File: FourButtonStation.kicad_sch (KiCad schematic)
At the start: 63 parts, among them J1 AC IN, J10 AC IN, J2 External 3V, J3 UART, J4 ADC, J5 Conn_WallSocket, J6 USB_B_Micro, J7 Conn_WallSocket, J8 Conn_WallSocket, J9 Conn_WallSocket, K1 G5LE-1, K2 G5LE-1, K3 G5LE-1, K4 G5LE-1, Q1 MMBT3904, Q3 MMBT3904, SW1 POWER, SW2 RST, SW5 Mode, U1 CH340C, U10 SM4007PL, U11 D882_C9634, U13 AMS1117-3_3, U2 radio-receiver, U3 ESP-07, U4 SM4007PL, U5 D882_C9634, U6 SM4007PL, U7 D882_C9634, U8 SM4007PL, U9 D882_C9634

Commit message: Update schematic
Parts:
- added C7: 1u, jlc_footprints:C0603, symbol jlc_symbols:CL10A105KB8NNNC
- added R14: 10k, jlc_footprints:R0603, symbol jlc_symbols:0603WAF1002T5E
- J1: footprint c8-inlet:c8-inlet -> c8-inlet:c8-inlet-old
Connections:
- net GND: now also C7.1, R14.1
- net RadioC: now also R14.2
- net at R13.1, U3.3 (EN): now also C7.2
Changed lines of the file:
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@@
   (junction (at 121.285 72.39) (diameter 0) (color 0 0 0 0)
   )
+  (junction (at 267.97 59.69) (diameter 0) (color 0 0 0 0)
+  )
   (junction (at 43.815 159.385) (diameter 0) (color 0 0 0 0)
   )
@@
   (junction (at 34.925 90.805) (diameter 0) (color 0 0 0 0)
   )
+  (junction (at 218.44 41.91) (diameter 0) (color 0 0 0 0)
+  )
   (junction (at 100.965 38.735) (diameter 0) (color 0 0 0 0)
   )
@@
     (stroke (width 0) (type default))
   )
+  (wire (pts (xy 267.97 59.69) (xy 270.51 59.69))
+    (stroke (width 0) (type default))
+  )
   (wire (pts (xy 43.815 69.215) (xy 43.815 70.485))
     (stroke (width 0) (type default))
@@
     (stroke (width 0) (type default))
   )
+  (wire (pts (xy 256.54 59.69) (xy 267.97 59.69))
+    (stroke (width 0) (type default))
+  )
   (wire (pts (xy 117.475 38.735) (xy 123.825 38.735))
     (stroke (width 0) (type default))
@@
     )
   )
-  (global_label "RadioC" (shape input) (at 256.54 59.69 0) (fields_autoplaced)
+  (global_label "RadioC" (shape input) (at 270.51 59.69 0) (fields_autoplaced)
     (effects (font (size 1.27 1.27)) (justify left))
-    (property "Intersheetrefs" "${INTERSHEET_REFS}" (at 265.545 59.7694 0)
+    (property "Intersheetrefs" "${INTERSHEET_REFS}" (at 279.515 59.7694 0)
       (effects (font (size 1.27 1.27)) (justify left) hide)
     )
@@
     )
   )
+  (symbol (lib_id "power:GND") (at 218.44 52.07 0) (unit 1)
+    (in_bom yes) (on_board yes) (dnp no)
+    (property "Reference" "#PWR042" (at 218.44 58.42 0)
+      (effects (font (size 1.27 1.27)) hide)
+    )
+    (property "Value" "GND" (at 218.44 59.69 90)
+      (effects (font (size 1.27 1.27)) (justify left))
+    )
+    (property "Footprint" "" (at 218.44 52.07 0)
+      (effects (font (size 1.27 1.27)) hide)
+    )
+    (property "Datasheet" "" (at 218.44 52.07 0)
+      (effects (font (size 1.27 1.27)) hide)
+    )
+    (pin "1")
+    (instances
+      (project "FourButtonStation"
+        (path "/fe8954b5-d30a-4533-a19e-bff77a7cd4d5"
+          (reference "#PWR042") (unit 1)
+        )
+      )
+    )
+  )
   (symbol (lib_id "Graphic:SYM_Flash_XLarge") (at 80.645 110.49 0) (unit 1)
     (in_bom no) (on_board no) (dnp no) (fields_autoplaced)
@@
     )
   )
+  (symbol (lib_id "jlc_symbols:0603WAF1002T5E") (at 267.97 64.77 90) (unit 1)
+    (in_bom yes) (on_board yes) (dnp no) (fields_autoplaced)
+    (property "Reference" "R14" (at 270.51 63.5 90)
+      (effects (font (size 1.27 1.27)) (justify right))
+    )
+    (property "Value" "10k" (at 270.51 66.04 90)
+      (effects (font (size 1.27 1.27)) (justify right))
+    )
+    (property "Footprint" "jlc_footprints:R0603" (at 278.13 64.77 0)
+      (effects (font (size 1.27 1.27) italic) hide)
+    )
+    (property "Datasheet" "https://www.mouser.in/datasheet/2/447/PYu_RT_1_to_0_01_RoHS_L_11-1669912.pdf" (at 267.843 67.056 0)
+      (effects (font (size 1.27 1.27)) (justify left) hide)
+    )
+    (property "LCSC" "C25804" (at 267.97 64.77 0)
+      (effects (font (size 1.27 1.27)) hide)
+    )
+    (pin "1")
+    (pin "2")
+    (instances
+      (project "FourButtonStation"
+        (path "/fe8954b5-d30a-4533-a19e-bff77a7cd4d5"
+          (reference "R14") (unit 1)
+        )
+      )
+    )
+  )
   (symbol (lib_id "Transistor_BJT:MMBT3904") (at 254 127.635 180) (unit 1)
     (in_bom yes) (on_board yes) (dnp no) (fields_autoplaced)
@@
   )
   (symbol (lib_id "CL05A106MQ5NUNC:CL05A106MQ5NUNC") (at 208.28 40.64 90) (unit 1)
-    (in_bom yes) (on_board yes) (dnp no) (fields_autoplaced)
-    (property "Reference" "C6" (at 212.09 39.3699 90)
+    (in_bom yes) (on_board yes) (dnp no)
+    (property "Reference" "C6" (at 210.82 39.37 90)
       (effects (font (size 1.27 1.27)) (justify right))
     )
-    (property "Value" "10u" (at 212.09 41.9099 90)
+    (property "Value" "10u" (at 210.82 41.91 90)
       (effects (font (size 1.27 1.27)) (justify right))
     )
@@
     )
   )
+  (symbol (lib_id "jlc_symbols:CL10A105KB8NNNC") (at 218.44 46.99 90) (unit 1)
+    (in_bom yes) (on_board yes) (dnp no)
+    (property "Reference" "C7" (at 213.36 45.72 90)
+      (effects (font (size 1.27 1.27)) (justify right))
+    )
+    (property "Value" "1u" (at 213.36 48.26 90)
+      (effects (font (size 1.27 1.27)) (justify right))
+    )
+    (property "Footprint" "jlc_footprints:C0603" (at 228.6 46.99 0)
+      (effects (font (size 1.27 1.27) italic) hide)
+    )
+    (property "Datasheet" "https://item.szlcsc.com/362304.html" (at 218.313 49.276 0)
+      (effects (font (size 1.27 1.27)) (justify left) hide)
+    )
+    (property "LCSC" "C15849" (at 218.44 46.99 0)
+      (effects (font (size 1.27 1.27)) hide)
+    )
+    (pin "2")
+    (pin "1")
+    (instances
+      (project "FourButtonStation"
+        (path "/fe8954b5-d30a-4533-a19e-bff77a7cd4d5"
+          (reference "C7") (unit 1)
+        )
+      )
+    )
+  )
   (symbol (lib_id "jlc_symbols:SM4007PL") (at 34.925 168.275 270) (unit 1)
     (in_bom yes) (on_board yes) (dnp no)
@@
       (effects (font (size 1.27 1.27)) (justify right))
     )
-    (property "Footprint" "c8-inlet:c8-inlet" (at 117.1194 63.1952 0)
+    (property "Footprint" "c8-inlet:c8-inlet-old" (at 117.1194 63.1952 0)
       (effects (font (size 1.27 1.27)) hide)
     )
@@
         )
       )
+    )
+  )
+  (symbol (lib_id "power:GND") (at 267.97 69.85 0) (unit 1)
+    (in_bom yes) (on_board yes) (dnp no)
+    (property "Reference" "#PWR041" (at 267.97 76.2 0)
+      (effects (font (size 1.27 1.27)) hide)
+    )
+    (property "Value" "GND" (at 267.97 77.47 90)
+      (effects (font (size 1.27 1.27)) (justify left))
+    )
+    (property "Footprint" "" (at 267.97 69.85 0)
+      (effects (font (size 1.27 1.27)) hide)
+    )
+    (property "Datasheet" "" (at 267.97 69.85 0)
+      (effects (font (size 1.27 1.27)) hide)
+    )
+    (pin "1")
+    (instances
+      (project "FourButtonStation"
+        (path "/fe8954b5-d30a-4533-a19e-bff77a7cd4d5"
+          (reference "#PWR041") (unit 1)
+        )
+      )

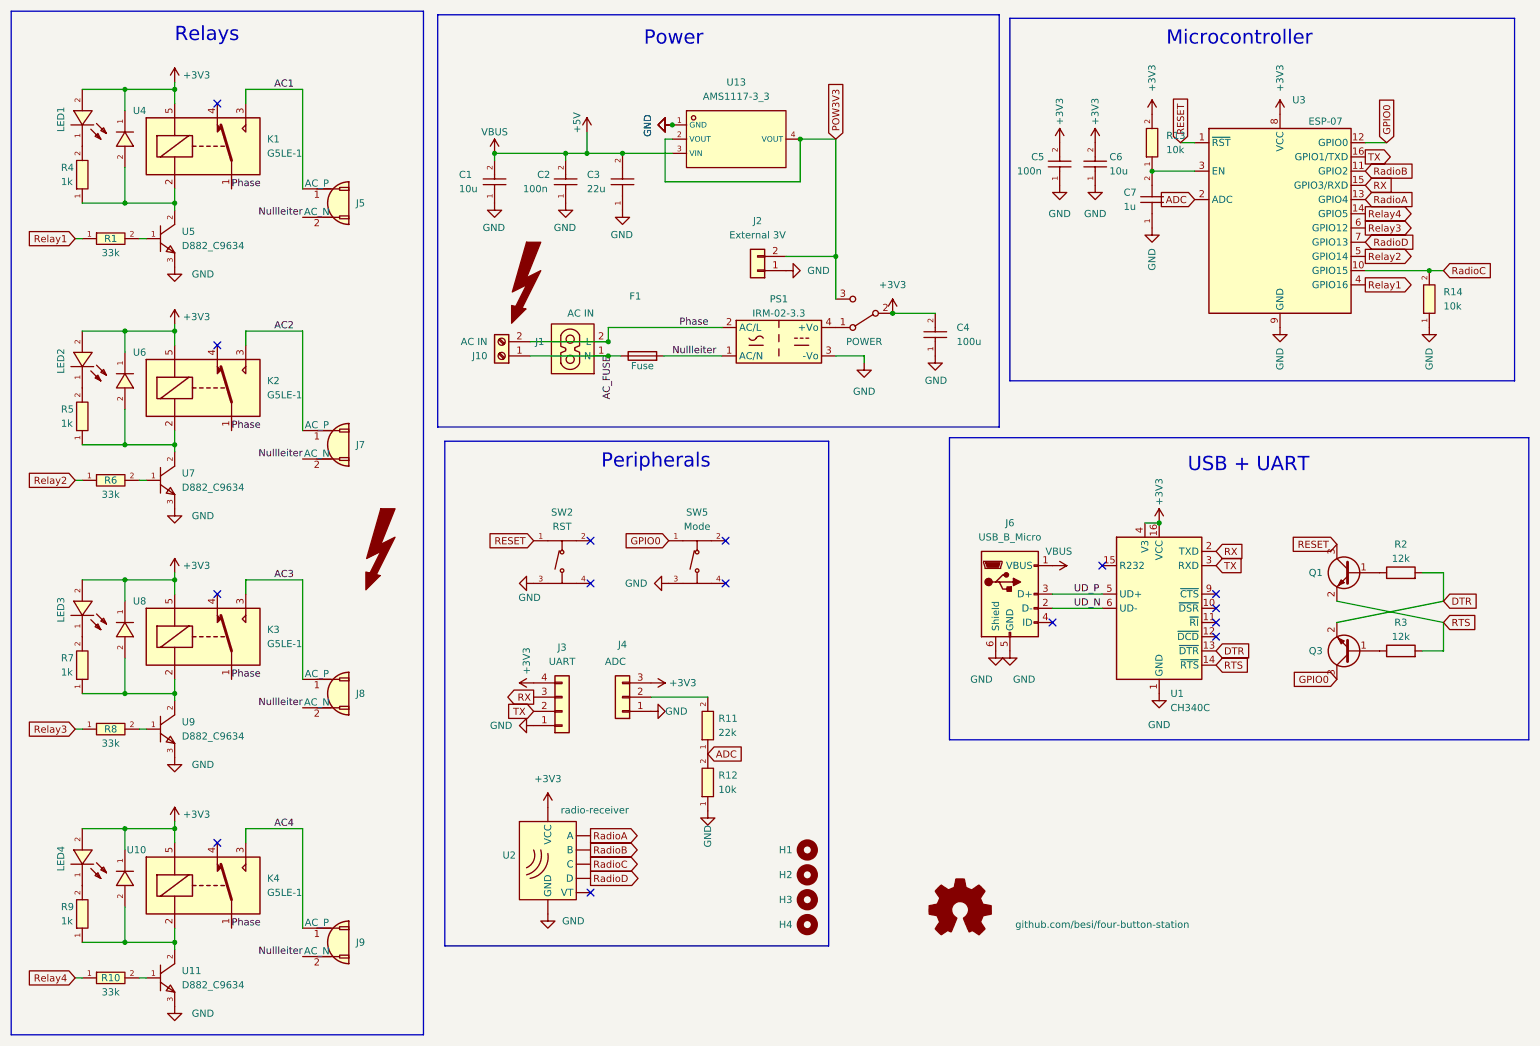
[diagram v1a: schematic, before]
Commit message: Re-arrange elements in Schematic to match the grid
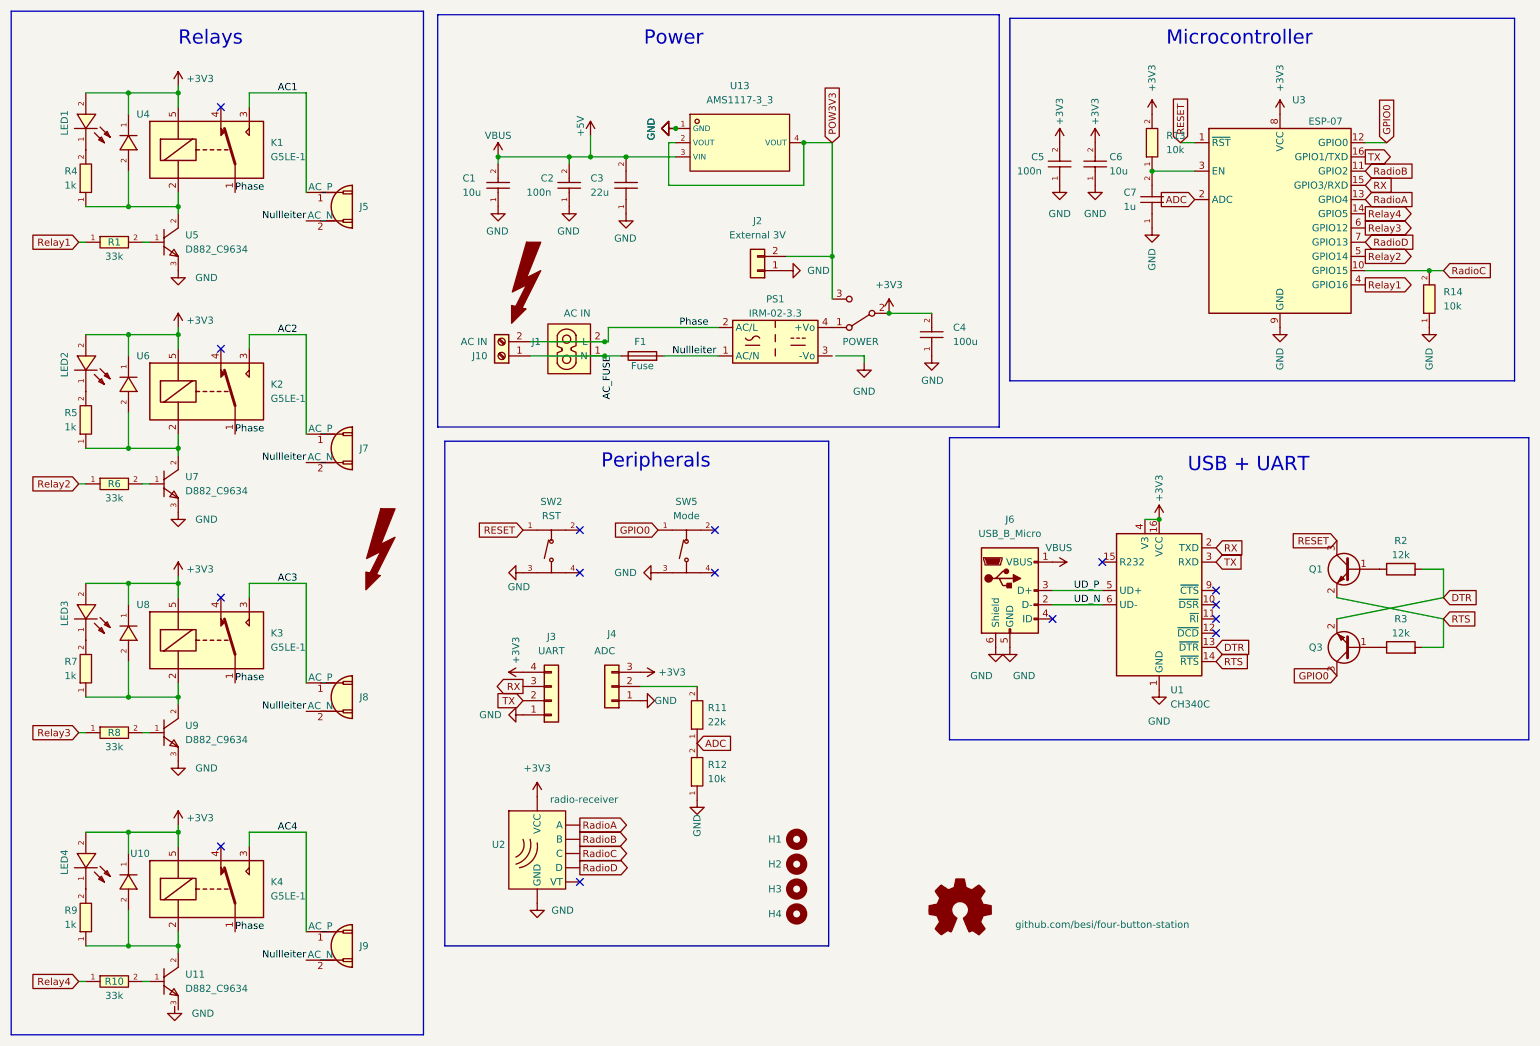
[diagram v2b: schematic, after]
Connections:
- net GND: no longer PS1.3 (-Vo), U11.3 (E)
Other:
- moved on the sheet: C1, C2, C3, C4, H1, H2, H3, H4, J1, J3, J4, J5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

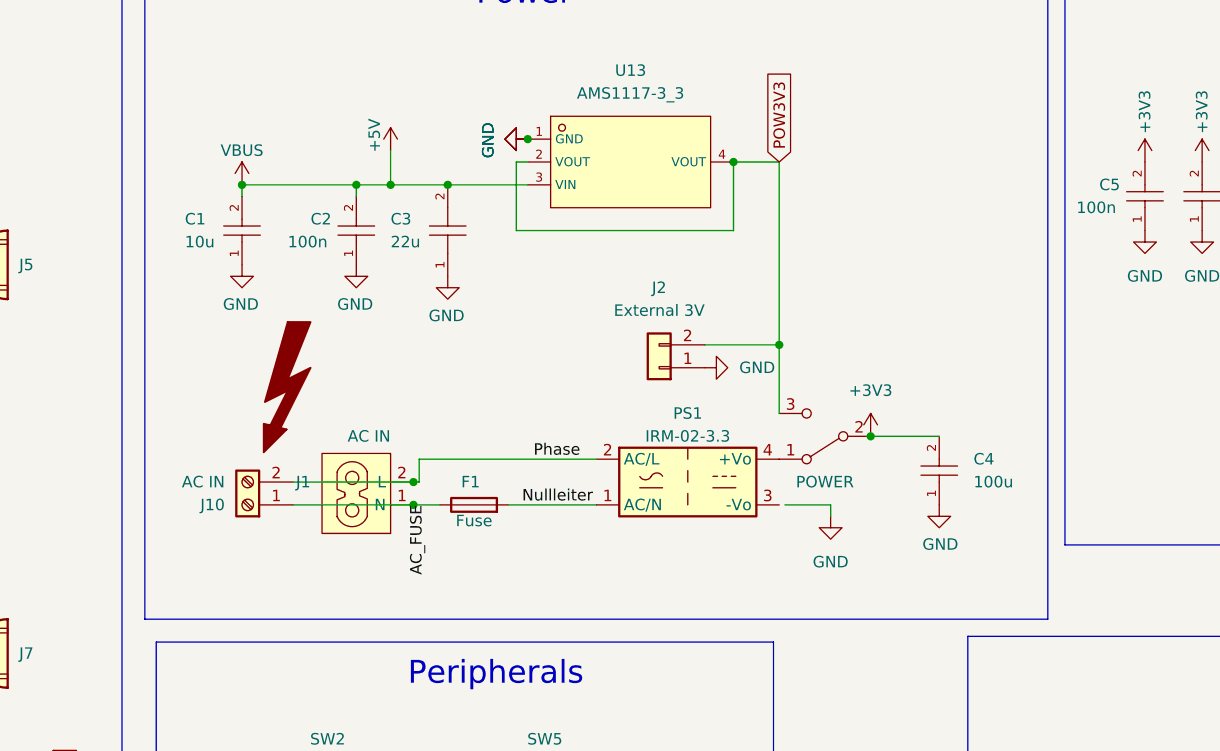
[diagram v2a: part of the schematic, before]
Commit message: Add another C8 Power entry AC plug as an option
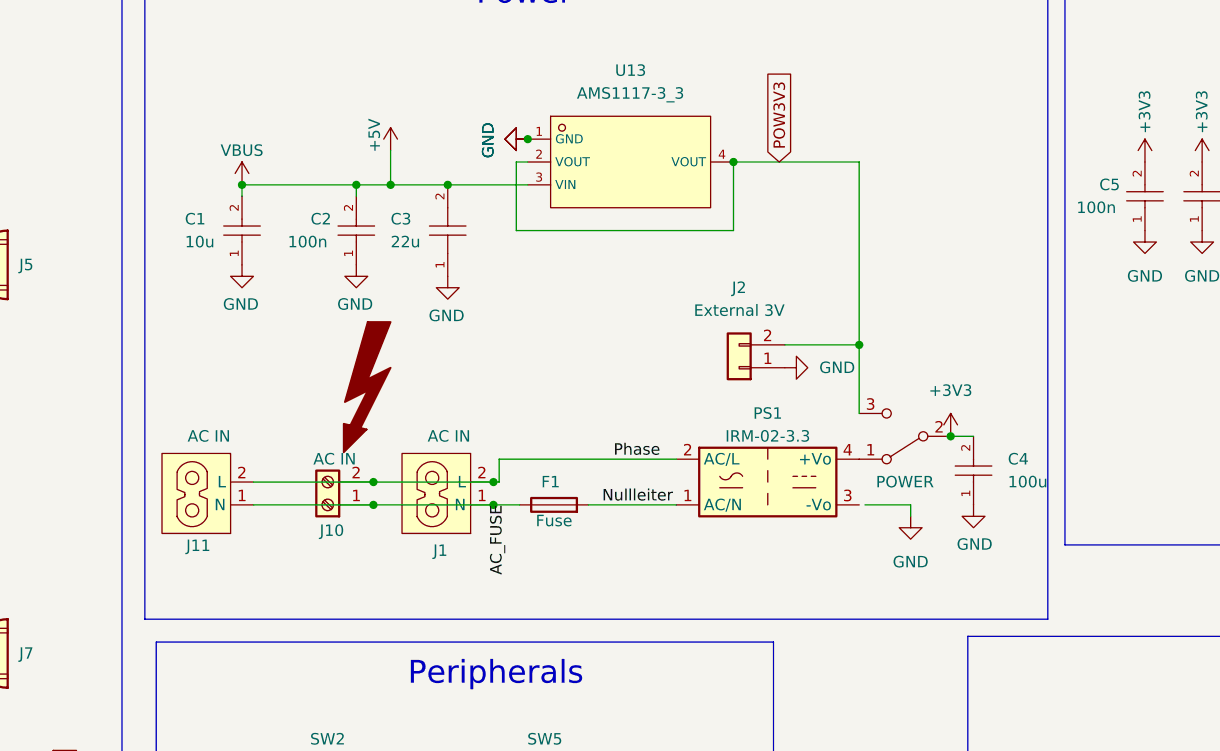
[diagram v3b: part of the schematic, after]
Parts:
- added J11: AC IN, c8-inlet:c8-inlet, symbol c8-inlet:c8-inlet
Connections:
- net AC_FUSE: now also J11.1 (N)
- net Phase: now also J11.2 (L)
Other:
- moved on the sheet: C4, F1, J1, J10, J2, PS1
